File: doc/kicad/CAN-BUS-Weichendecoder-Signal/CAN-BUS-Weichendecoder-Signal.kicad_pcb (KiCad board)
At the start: 2 copper layers, 58.4 x 127 mm, 41 parts, among them J1 Conn_01x04_Male, J11 250-1406, J12 Wago 250-1406, J13 Wago 250-1406, J14 Wago 250-1406, J15 Wago 250-1406, J16 Wago 250-1406, J21 Conn_01x06, J22 Conn_01x06, J23 Conn_01x06, J24 Conn_01x06, J25 Conn_01x06, J26 Conn_01x06, J31 RJ12, J32 RJ12, J33 RJ12, J34 RJ12, J35 RJ12, J36 RJ12, J5 Conn_01x03, U1 PCF8574, U2 PCF8574, U3 PCF8574, U4 PCF8574, U5 ULN2803A, U6 ULN2803A, U7 ULN2803A, U8 ULN2803A

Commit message: Lage der Stecker angepasst
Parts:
- moved J12 0.70 mm to (78.9, 129.5)
- moved J11 0.69 mm to (78.7, 149.8)
- moved J31 0.63 mm to (72.9, 147.3)
- moved J32 0.63 mm to (72.9, 127.0)
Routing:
- net Net-(JP1-Pad2): track 105.1 -> 102.8 mm
- net Net-(J12-Pad6): track 45.0 -> 43.5 mm
- net Net-(J12-Pad2): track 31.1 -> 29.5 mm
- net Net-(J13-Pad2): track 27.7 -> 29.0 mm
- net Net-(J12-Pad5): track 40.8 -> 39.7 mm
- net Net-(J14-Pad6): track 42.2 -> 43.0 mm
- net Net-(J11-Pad6): track 43.0 -> 42.3 mm
- net Net-(J13-Pad6): track 41.4 -> 42.1 mm
- net Net-(J11-Pad4): track 27.2 -> 26.7 mm
- net Net-(J11-Pad3): track 24.1 -> 23.6 mm

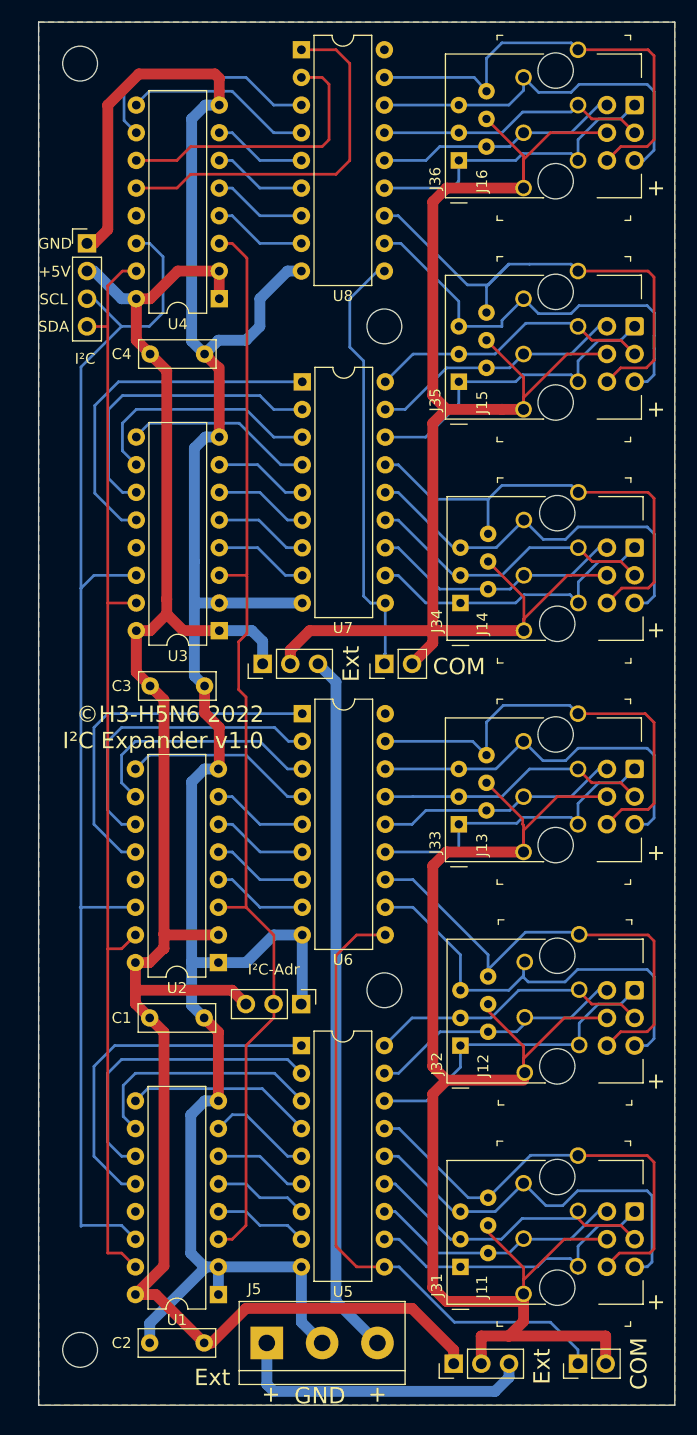
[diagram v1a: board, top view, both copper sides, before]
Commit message: i2c-Adresse bewchriftet, RJ12 neu ausgerichtet
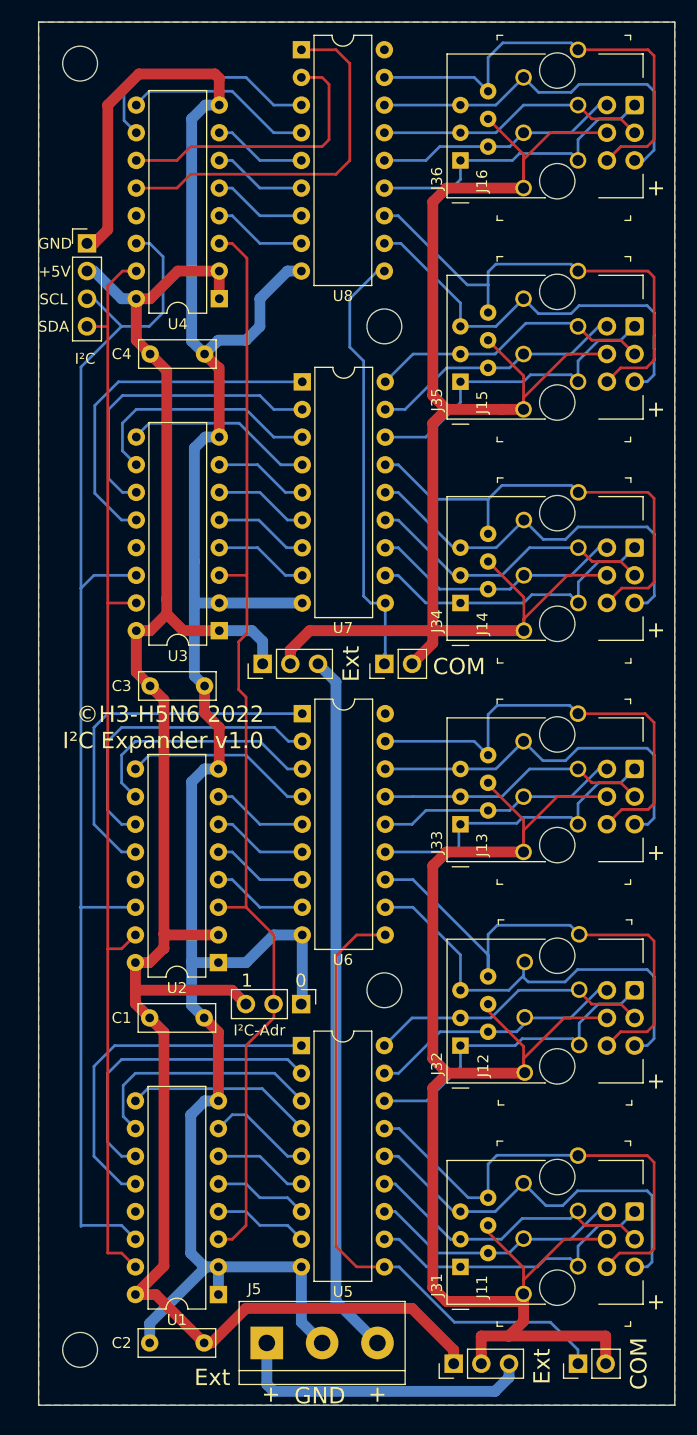
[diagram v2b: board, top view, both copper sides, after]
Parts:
- moved J33 0.15 mm to (72.9, 106.7)
- moved J35 0.15 mm to (72.9, 66.0)
- moved J36 0.15 mm to (72.9, 45.7)
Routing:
- net Net-(J12-Pad6): track 43.5 -> 47.2 mm
- net Net-(J15-Pad6): track 46.7 -> 44.7 mm
- net Net-(J11-Pad6): track 42.3 -> 44.1 mm
- net Net-(J11-Pad1): track 139.0 -> 138.0 mm
- net Net-(J16-Pad5): track 35.2 -> 34.5 mm
- net Net-(J11-Pad2): track 28.5 -> 27.8 mm
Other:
- board text added: "0"
- board text added: "1"

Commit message: Version auf 1.1 geändert + Kosmetik
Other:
- board text added: "©H3-H5N6 2022 I²C Expander v1.1"
- board text removed: "©H3-H5N6 2022 I²C Expander v1.0"
